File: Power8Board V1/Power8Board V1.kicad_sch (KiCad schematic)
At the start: 35 parts, among them J0 XT30, J1 XT30, J10 XT60IPW-M, J2 XT30, J3 XT30, J4 XT30, J5 XT30, J6 XT30, J7 XT30, J8 Qwiic_RA

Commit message: Added power indicator LEDs.
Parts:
- added D1: Amber, 0805 LED:WL-SMCW_0805, symbol Device:LED
- added D2: Red, 0805 LED:WL-SMCW_0805, symbol Device:LED
- added D3: Yellow, 0805 LED:WL-SMCW_0805, symbol Device:LED
- added D4: Green, 0805 LED:WL-SMCW_0805, symbol Device:LED
- added R21: 680, Resistor_SMD:R_0805_2012Metric, symbol Device:R
- added R22: 2.2k, Resistor_SMD:R_0805_2012Metric, symbol Device:R
- added R23: 1.2k, Resistor_SMD:R_0805_2012Metric, symbol Device:R
- added R24: 56k, Resistor_SMD:R_0805_2012Metric, symbol Device:R
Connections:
- net +12V: now also R22.1
- net +3.3V: now also R21.1
- net +48V: now also R24.1
- net +5V: now also R23.1
- net GND: now also D1.1 (K), D2.1 (K), D3.1 (K), D4.1 (K)
- new net: D2.2 (A), R23.2
- new net: D4.2 (A), R24.2
- new net: D1.2 (A), R21.2
- new net: D3.2 (A), R22.2
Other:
- moved on the sheet: J8

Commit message: Design before laying out.
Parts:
- J8: Mfr. (none) -> JST Sales America Inc.; Order Link (none) -> https://www.digikey.com/en/products/detail/jst-sales-americ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; PROD_ID CONN-13694 -> (none); Part # (none) -> SM04B-SRSS-TB; Price (none) -> $0.424
- R1, R2, R3: footprint (none) -> Resistor_SMD:R_0805_2012Metric; Mfr. (none) -> TE Connectivity; Order Link (none) -> https://www.digikey.com/en/products/detail/te-connectivity-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; Part # (none) -> CRGCQ0805F10K; Price (none) -> $0.036
- R4: footprint (none) -> Resistor_SMD:R_0805_2012Metric; Mfr. (none) -> TE Connectivity; Order Link (none) -> https://www.digikey.com/en/products/detail/te-connectivity-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; Part # (none) -> CRGCQ0805F470K; Price (none) -> $0.036

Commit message: Beginning to layout.
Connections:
- net +12V/0: now also J0.2 (POS); no longer J0.P (POS)
- net +12V/1: now also J1.2 (POS); no longer J1.P (POS)
- net +12V/2: now also J2.2 (POS); no longer J2.P (POS)
- net +12V/3: now also J3.2 (POS); no longer J3.P (POS)
- net +12V/4: now also J4.2 (POS); no longer J4.P (POS)
- net +12V/5: now also J5.2 (POS); no longer J5.P (POS)
- net +12V/6: now also J6.2 (POS); no longer J6.P (POS)
- net +12V/7: now also J7.2 (POS); no longer J7.P (POS)
- net +48V: now also J10.2 (POS); no longer J10.P (POS)
- net GND: now also J0.1 (NEG), J1.1 (NEG), J10.1 (NEG), J2.1 (NEG), J3.1 (NEG), J4.1 (NEG), J5.1 (NEG), J6.1 (NEG), J7.1 (NEG); no longer J0.N (NEG), J1.N (NEG), J10.N (NEG), J2.N (NEG), J3.N (NEG), J4.N (NEG), J5.N (NEG), J6.N (NEG), J7.N (NEG)

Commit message: There is a general layout.
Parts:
- removed C6: 56 uF, PCR1J560MCL1GS:CAP_PC_8X12_NCH, symbol Device:C_Polarized
- added J9: MR30PW-M, Connector_AMASS:AMASS_MR30PW-M_1x03_P3.50mm_Horizontal, symbol Connector_Generic:Conn_01x03
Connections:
- net +12V: now also J9.1 (Pin_1)
- net +5V: now also J9.3 (Pin_3)
- net GND: now also J9.2 (Pin_2)

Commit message: Laid out components
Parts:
- removed C10, C8: 0.1 uF, 0805 Ceramic Capacitor:CAPC2012X140N, symbol Device:C_Small
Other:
- moved on the sheet: C9

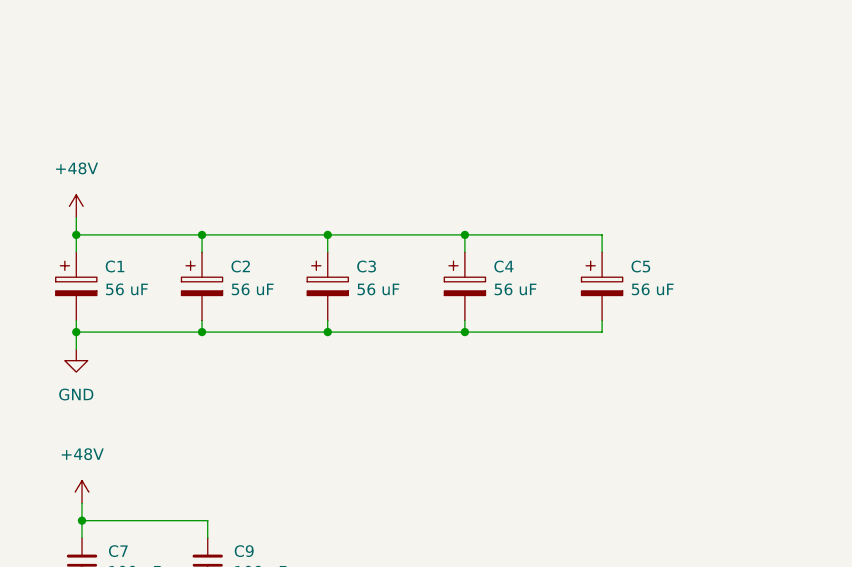
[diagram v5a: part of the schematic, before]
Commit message: Switched out input capacitors.
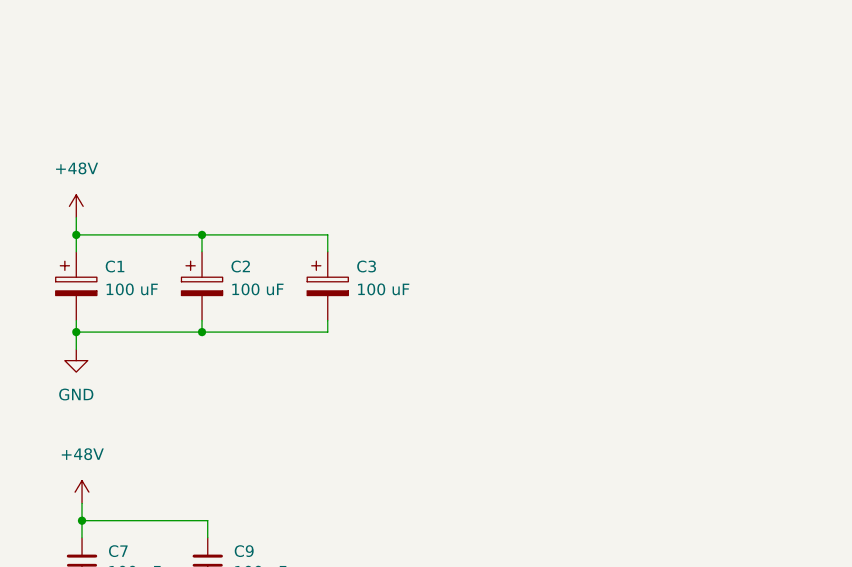
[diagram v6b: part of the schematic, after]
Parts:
- removed C4, C5: 56 uF, PCR1J560MCL1GS:CAP_PC_8X12_NCH, symbol Device:C_Polarized
- C1, C2, C3: value 56 uF -> 100 uF; footprint PCR1J560MCL1GS:CAP_PC_8X12_NCH -> 107AVG063MFBJ:CAP_AVG-8x12_ILC; Mfr. Nichicon -> Cornell Dubilier Knowles; Order Link https://www.digikey.com/en/products/detail/nichicon/PCR1J56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 -> https://www.digikey.com/en/products/detail/cornell-dubilier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; Part # PCR1J560MCL1GS -> 107AVG063MFBJ; Price $1.957 -> $2.71

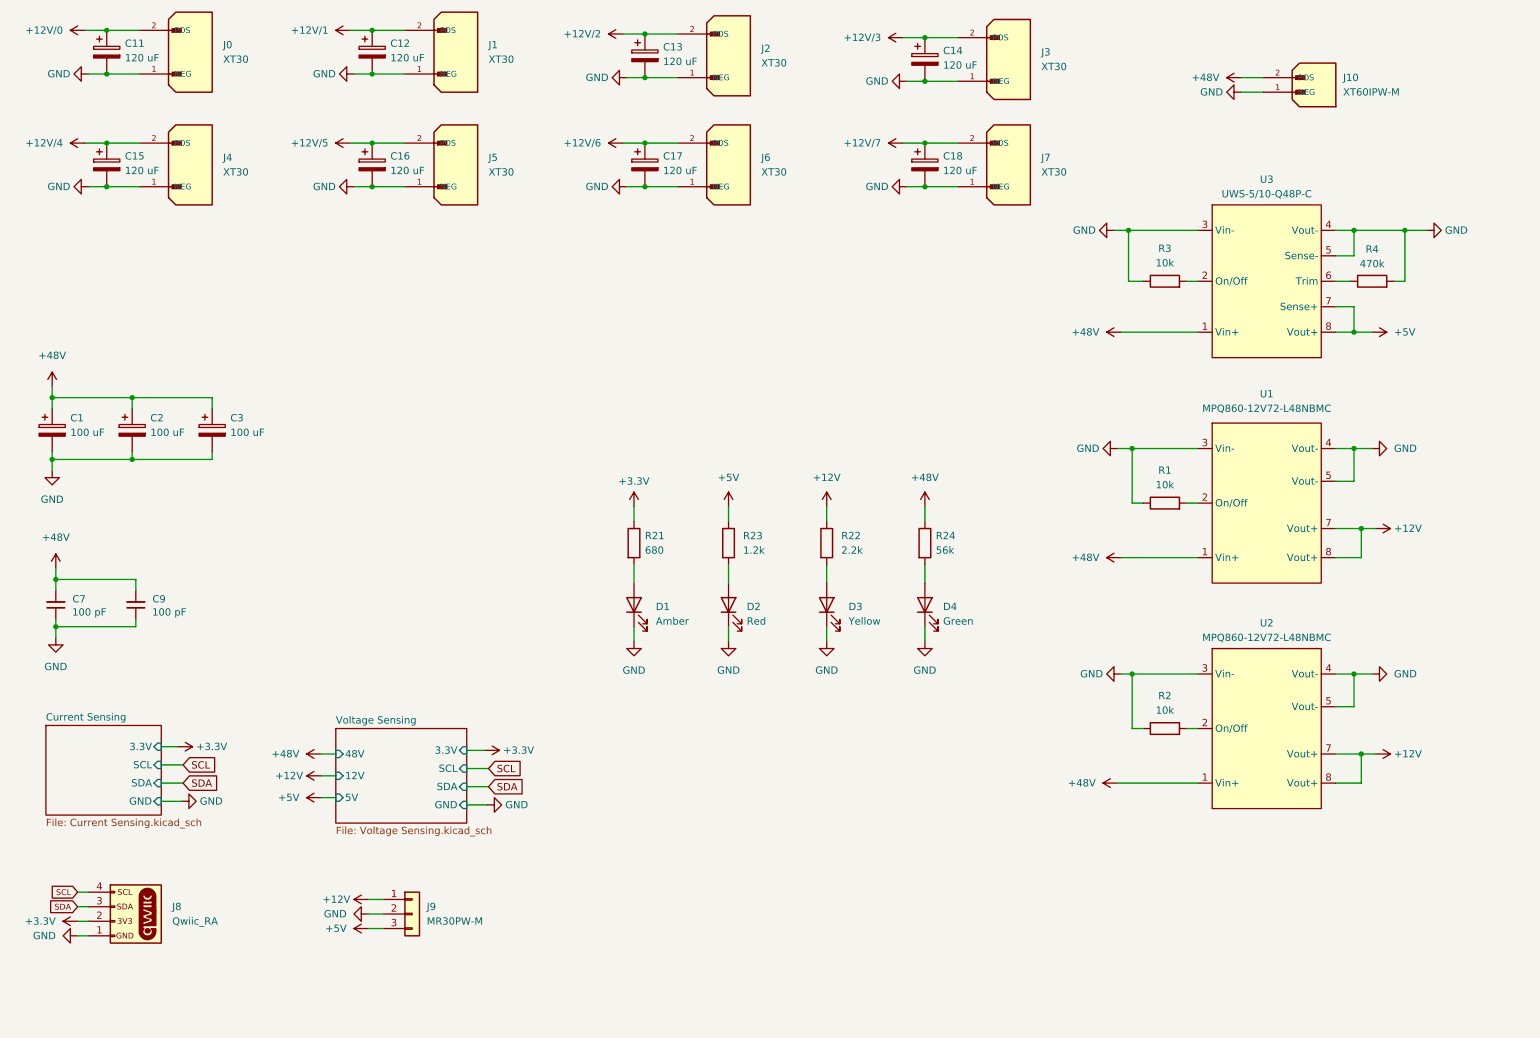
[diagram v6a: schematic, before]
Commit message: Added boxes in schematic for organization.
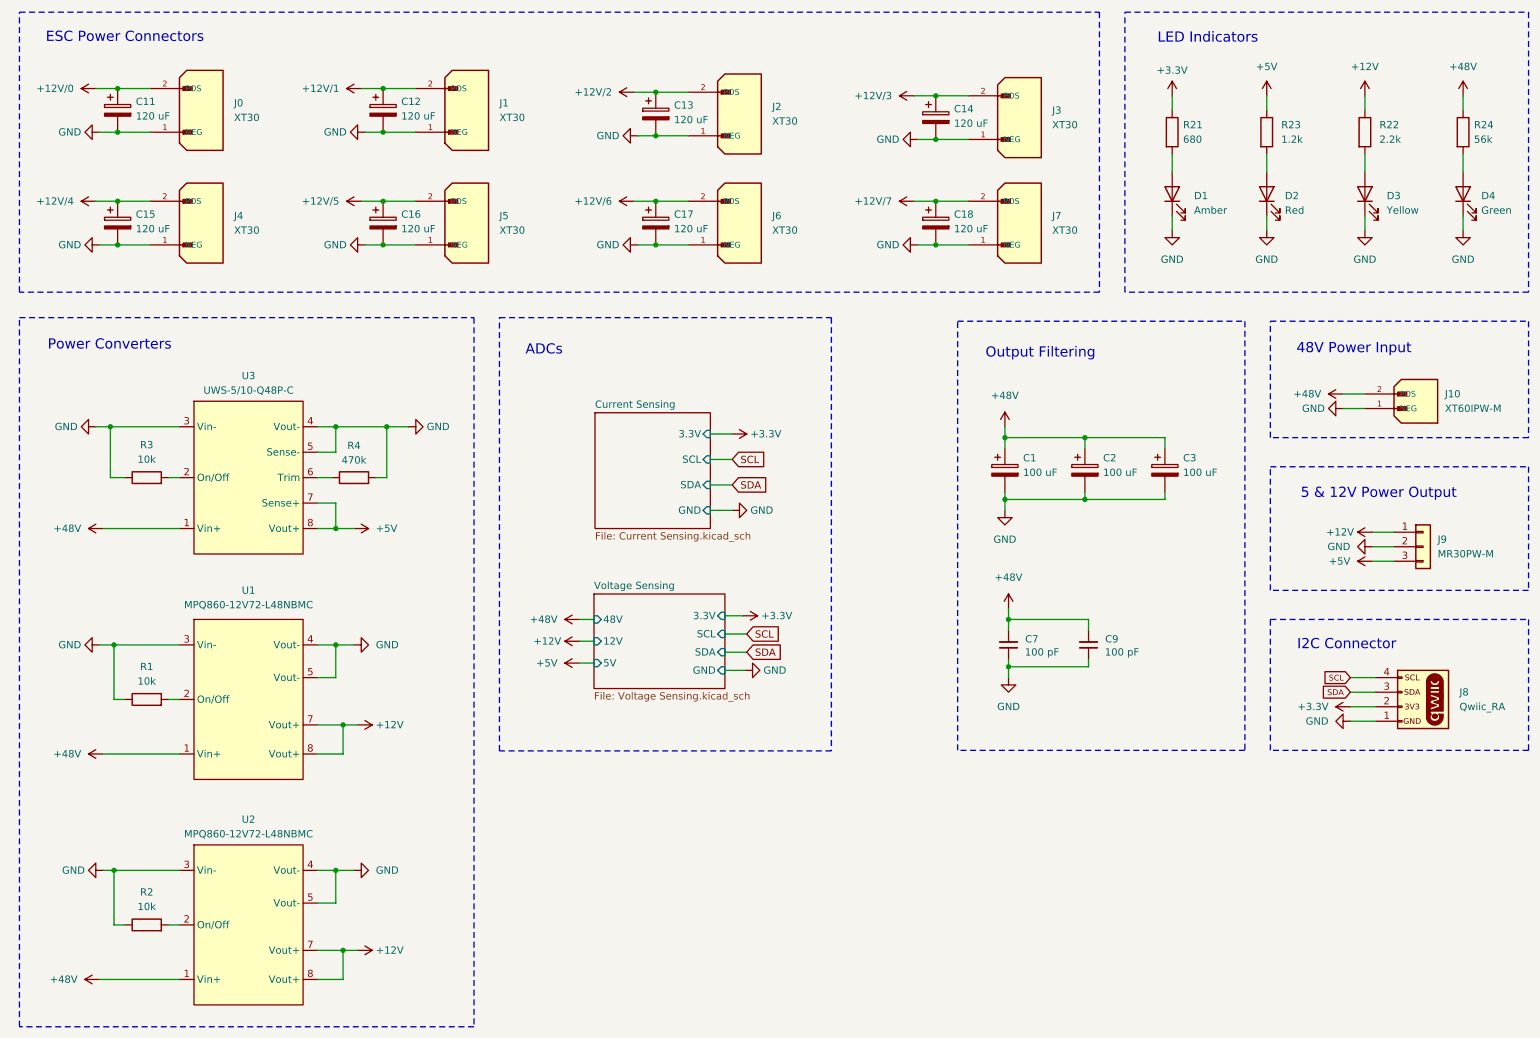
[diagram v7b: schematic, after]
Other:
- note added: "48V Power Input"
- note added: "5 & 12V Power Output"
- note added: "ADCs"
- note added: "ESC Power Connectors"
- note added: "I2C Connector"
- note added: "LED Indicators"
- note added: "Output Filtering"
- note added: "Power Converters"
- company: (none) -> Rovotics
- title: (none) -> Power8Board
- moved on the sheet: C1, C11, C12, C13, C14, C15, C16, C17, C18, C2, C3, C7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

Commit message: Added non KiCad standard components in Components folder.
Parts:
- U3: footprint UWS-5_10-Q48P-C:UWS-5_10-Q48P-C -> UWS-5_10-Q48:UWS-5_10-Q48
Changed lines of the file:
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@@
 			)
 		)
-		(property "Footprint" "UWS-5_10-Q48P-C:UWS-5_10-Q48P-C"
+		(property "Footprint" "UWS-5_10-Q48:UWS-5_10-Q48"
 			(at 56.515 97.79 0)
 			(effects
